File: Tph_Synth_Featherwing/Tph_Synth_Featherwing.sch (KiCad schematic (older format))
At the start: 3 parts, among them J1 AudioJack3, J2 Conn_01x04

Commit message: Added BOM and upgraded to kicad 5.0
Signed-off-by: Tisham Dhar <whatnickd@gmail.com>
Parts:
- J1: manf# (none) -> SJ-3523-SMT-TR
- J2: manf# (none) -> 105314-1204
- LOGO1: DNP (none) -> (none)
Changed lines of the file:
@@
 EESchema Schematic File Version 4
-LIBS:Tph_Synth_Featherwing-cache
-EELAYER 26 0
+EELAYER 30 0
 EELAYER END
 $Descr A4 11693 8268
@@
 F 2 "Connector_Molex:Molex_Nano-Fit_105314-xx04_2x02_P2.50mm_Horizontal" H 10020 3035 50  0001 C CNN
 F 3 "~" H 10020 3035 50  0001 C CNN
+F 4 "105314-1204" H 10020 3035 50  0001 C CNN "manf#"
 	1    10020 3035
 	1    0    0    -1
@@
 F 2 "Connector_Audio:Jack_3.5mm_CUI_SJ-3523-SMT_Horizontal" H 9955 4265 50  0001 C CNN
 F 3 "~" H 9955 4265 50  0001 C CNN
+F 4 "SJ-3523-SMT-TR" H 9955 4265 50  0001 C CNN "manf#"
 	1    9955 4265
 	-1   0    0    1
@@
 F 2 "Symbol:OSHW-Logo2_7.3x6mm_SilkScreen" H 7385 6865 50  0001 C CNN
 F 3 "~" H 7385 6865 50  0001 C CNN
+F 4 " " H 7385 6865 50  0001 C CNN "DNP"
 	1    7385 6865
 	1    0    0    -1

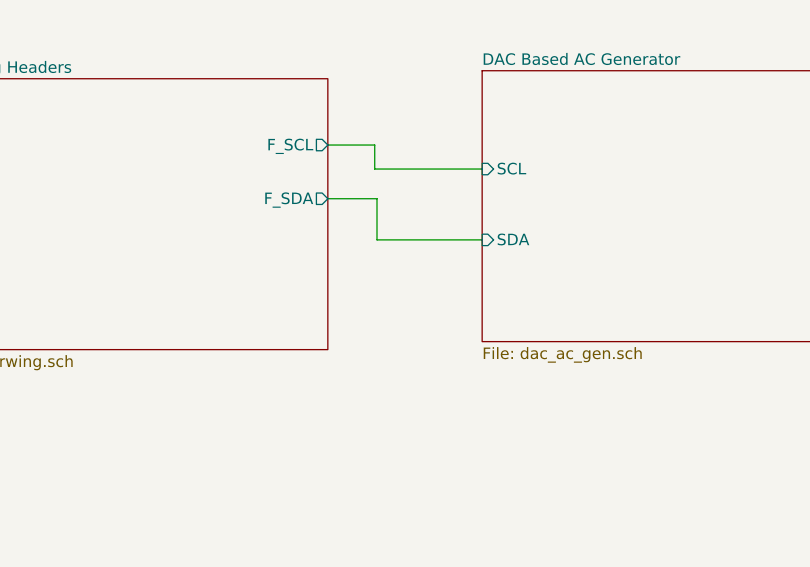
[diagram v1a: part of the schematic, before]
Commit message: #1 and #2 add mising wiring
Signed-off-by: Tisham Dhar <whatnickd@gmail.com>
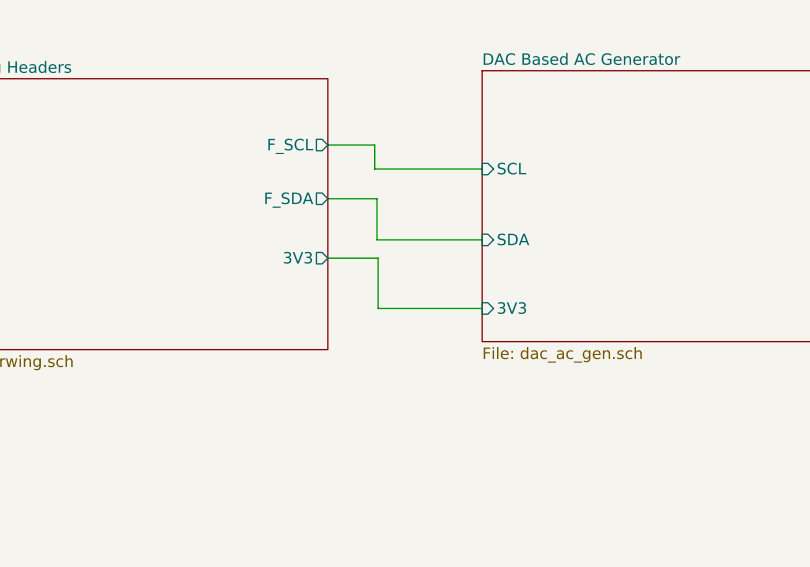
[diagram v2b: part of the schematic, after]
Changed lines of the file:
@@
 F6 "SCL" I L 3930 4360 50
 F7 "SDA" I L 3930 4670 50
+F8 "3V3" I L 3930 4970 50
 $EndSheet
 $Sheet
@@
 F4 "VBAT" O L 1430 4405 50
 F5 "VUSB" O L 1430 4120 50
+F6 "3V3" O R 3255 4750 50
 $EndSheet
 $Comp
@@
 	1    0    0    -1
 $EndComp
+Wire Wire Line
+	3475 4750 3475 4970
+Wire Wire Line
+	3475 4970 3930 4970
+Wire Wire Line
+	3255 4750 3475 4750
 $EndSCHEMATC
